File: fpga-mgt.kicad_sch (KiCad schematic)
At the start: 19 parts, among them U34 XCAU25P-2FFVB676I

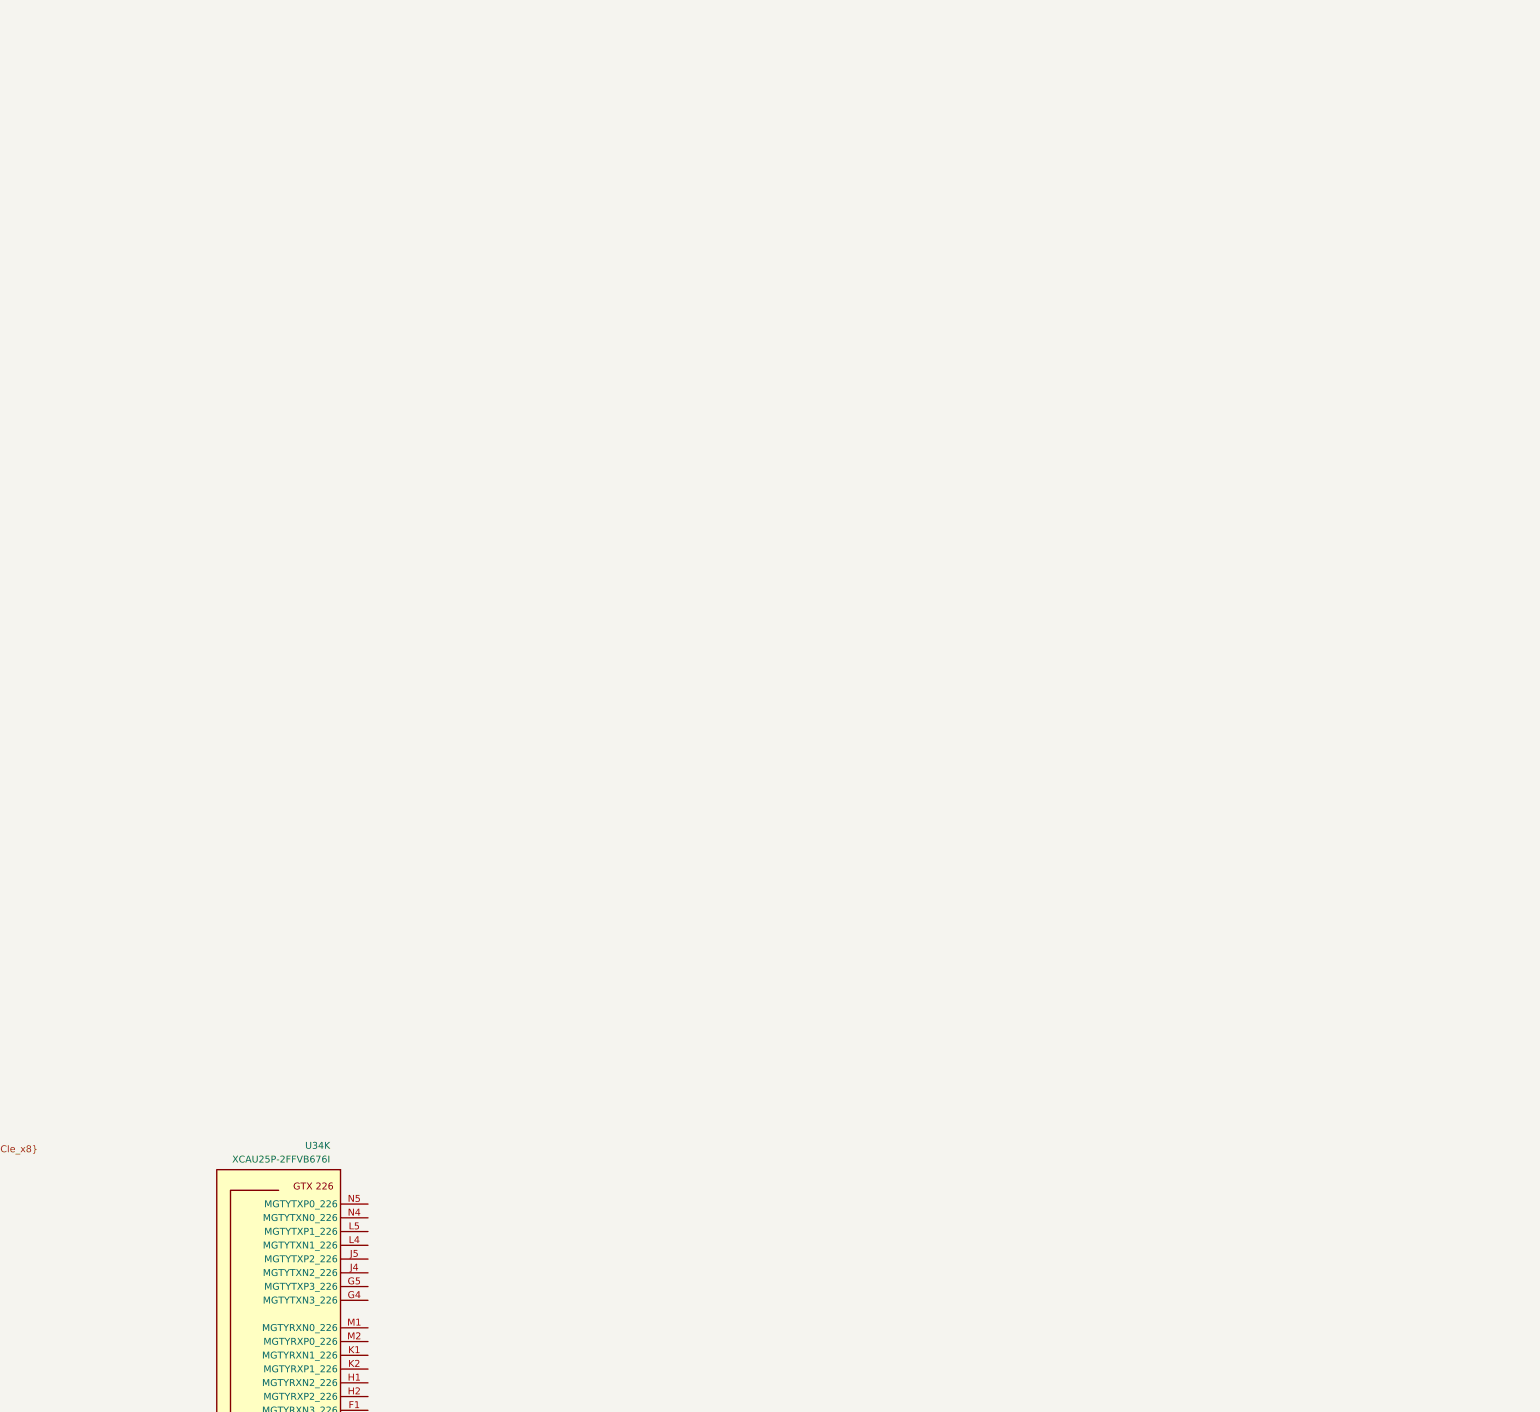
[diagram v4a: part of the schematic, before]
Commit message: [#66312] Add HDMI driver. Connect TMDS to GTH quad 226
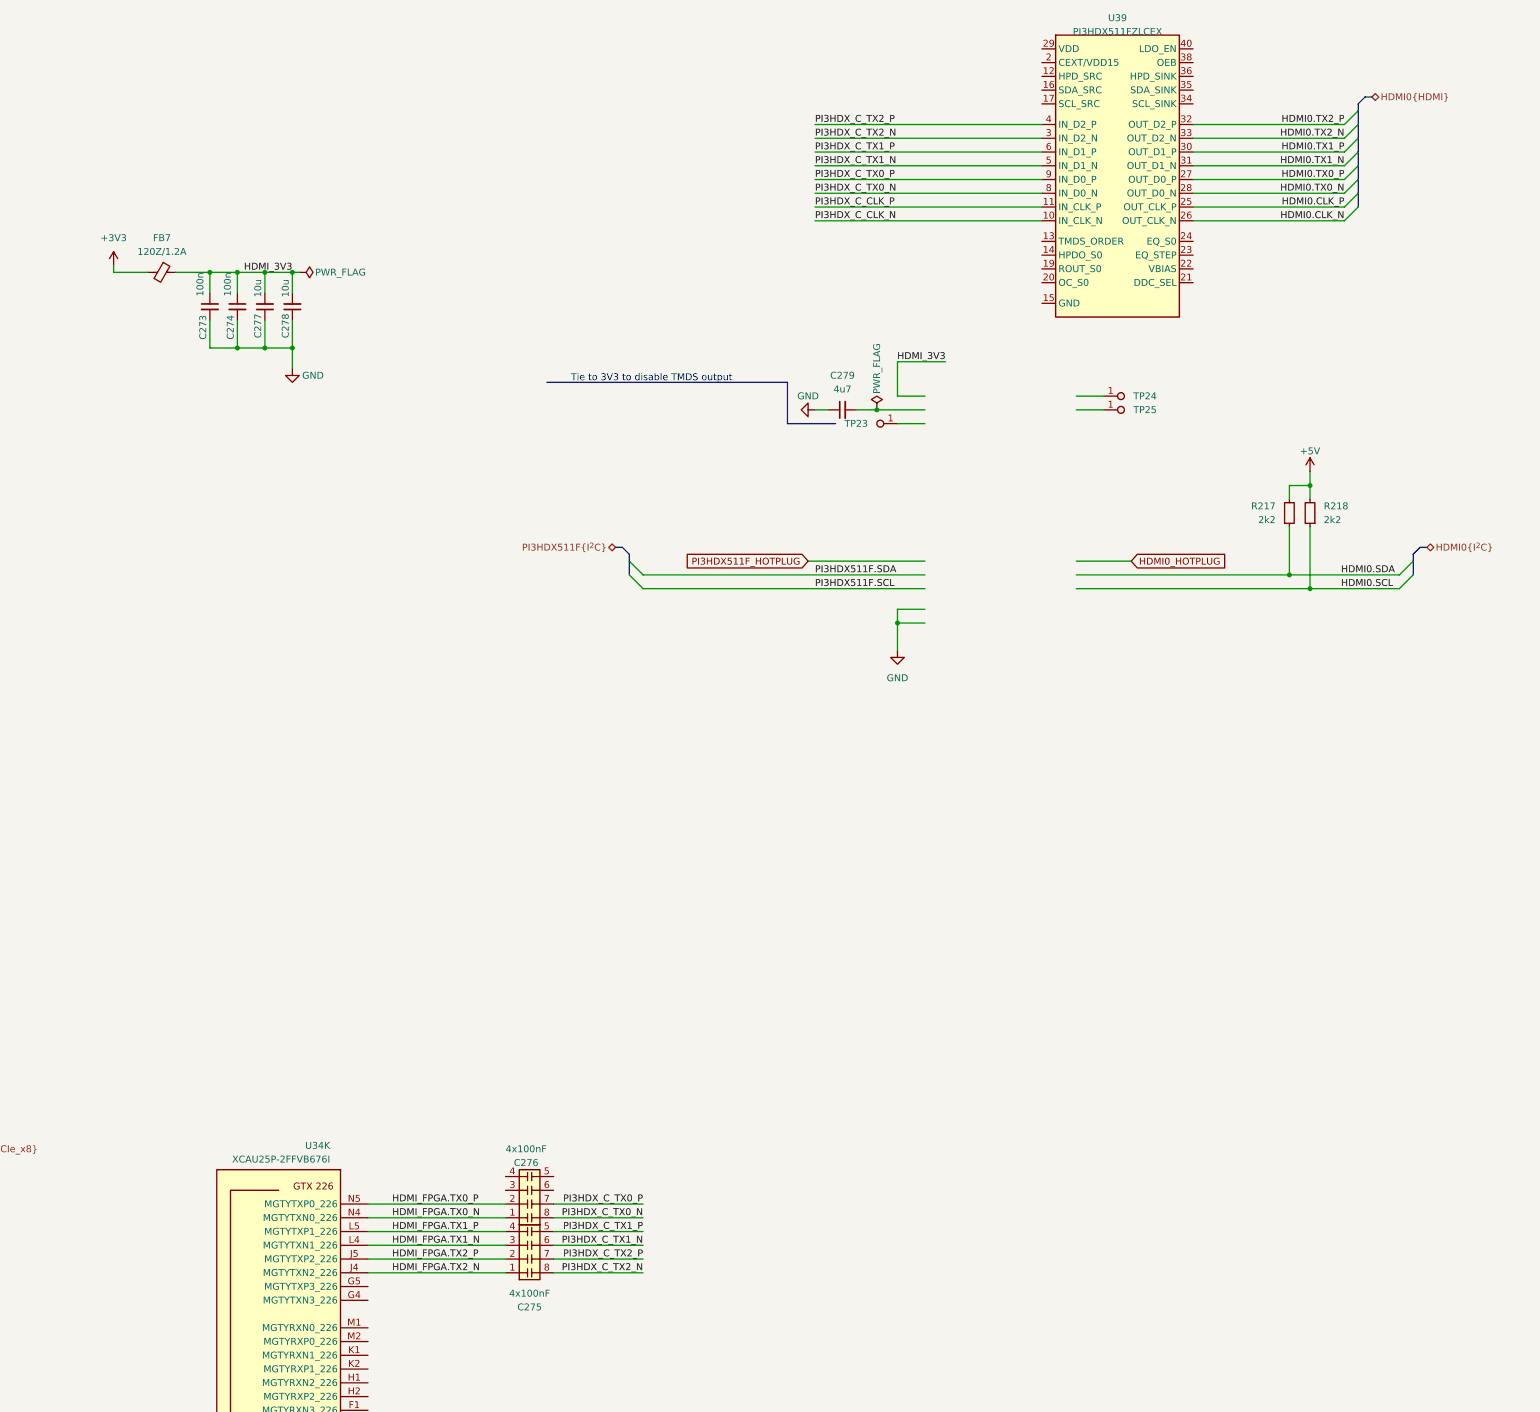
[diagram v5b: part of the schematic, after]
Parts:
- added C273, C274: C_100n_0402, antmicro-footprints:C_0402_1005Metric, symbol antmicroCapacitors0402:C_100n_0402
- added C275, C276: C_4x100nF_0508_1220Metric_array, antmicro-footprints:C_Array_0508_1220Metric, symbol antmicroCapacitorsmisc:C_4x100nF_0508_1220Metric_array
- added C277, C278: C_10u_10V_0402, antmicro-footprints:C_0402_1005Metric, symbol antmicroCapacitors0402:C_10u_10V_0402
- added C279: C_4u7_0402, antmicro-footprints:C_0402_1005Metric, symbol antmicroCapacitors0402:C_4u7_0402
- added FB7: FB_120Z_1.2A_TDK-MPZ_0402, antmicro-footprints:FB_0402_1005Metric, symbol antmicroFerriteBeadsandChips:FB_120Z_1.2A_TDK-MPZ_0402
- added R217, R218: R_2k2_0402, antmicro-footprints:R_0402_1005Metric, symbol antmicroResistors0402:R_2k2_0402
- added TP23, TP24, TP25: TP_0.75mm_SMD, antmicro-footprints:TP_SMD_0.75mm, symbol antmicroTestPoints:TP_0.75mm_SMD
- added U39: PI3HDX511FZLCEX, antmicro-footprints:QFN-40-1EP_3x6mm_Layout6x14, symbol antmicroInterfaceDriversReceiversTransceivers:PI3HDX511FZLCEX
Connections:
- net HDMI_FPGA.TX2_N: now reaches U34.J4 (MGTYTXN2_226)
- net HDMI_FPGA.TX2_N: now also C275.1 (R1.1)
- net HDMI_FPGA.TX2_P: now reaches U34.J5 (MGTYTXP2_226)
- net HDMI_FPGA.TX2_P: now also C275.2 (R2.1)
- net HDMI_FPGA.TX1_N: now reaches U34.L4 (MGTYTXN1_226)
- net HDMI_FPGA.TX1_N: now also C275.3 (R3.1)
- net HDMI_FPGA.TX1_P: now reaches U34.L5 (MGTYTXP1_226)
- net HDMI_FPGA.TX1_P: now also C275.4 (R4.1)
- net HDMI_FPGA.TX0_N: now reaches U34.N4 (MGTYTXN0_226)
- net HDMI_FPGA.TX0_N: now also C276.1 (R1.1)
- net HDMI_FPGA.TX0_P: now reaches U34.N5 (MGTYTXP0_226)
- net HDMI_FPGA.TX0_P: now also C276.2 (R2.1)
- new net +3V3: FB7.2
- new net +5V: R217.2, R218.2
- new net GND: C273.2, C274.2, C277.1, C278.1, C279.1, U39.15 (GND), U39.18 (GND), U39.37 (GND), U39.39 (GND), U39.41 (GND)
- new net HDMI0.CLK_N: U39.26 (OUT_CLK_N)
- new net HDMI0.CLK_P: U39.25 (OUT_CLK_P)
- new net HDMI0.SCL: R218.1
- new net HDMI0.SDA: R217.1
- new net HDMI0.TX0_N: U39.28 (OUT_D0_N)
- new net HDMI0.TX0_P: U39.27 (OUT_D0_P)
- new net HDMI0.TX1_N: U39.31 (OUT_D1_N)
- new net HDMI0.TX1_P: U39.30 (OUT_D1_P)
- new net HDMI0.TX2_N: U39.33 (OUT_D2_N)
- new net HDMI0.TX2_P: U39.32 (OUT_D2_P)
- new net HDMI_3V3: C273.1, C274.1, C277.2, C278.2, FB7.1
- new net PI3HDX_C_CLK_N: U39.10 (IN_CLK_N)
- new net PI3HDX_C_CLK_P: U39.11 (IN_CLK_P)
- new net PI3HDX_C_TX0_N: C276.8 (R1.2), U39.8 (IN_D0_N)
- new net PI3HDX_C_TX0_P: C276.7 (R2.2), U39.9 (IN_D0_P)
- new net PI3HDX_C_TX1_N: C275.6 (R3.2), U39.5 (IN_D1_N)
- new net PI3HDX_C_TX1_P: C275.5 (R4.2), U39.6 (IN_D1_P)
- new net PI3HDX_C_TX2_N: C275.8 (R1.2), U39.3 (IN_D2_N)
- new net PI3HDX_C_TX2_P: C275.7 (R2.2), U39.4 (IN_D2_P)
- new net VDD: U39.1 (VDD), U39.29 (VDD), U39.7 (VDD)
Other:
- note added: "Tie to 3V3 to disable TMDS output"

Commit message: [#66300] Replace HDMI output driver to SN75DP159
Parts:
- removed C277: C_10u_10V_0402, antmicro-footprints:C_0402_1005Metric, symbol antmicroCapacitors0402:C_10u_10V_0402
- removed FB7: FB_120Z_1.2A_TDK-MPZ_0402, antmicro-footprints:FB_0402_1005Metric, symbol antmicroFerriteBeadsandChips:FB_120Z_1.2A_TDK-MPZ_0402
- removed TP23: TP_0.75mm_SMD, antmicro-footprints:TP_SMD_0.75mm, symbol antmicroTestPoints:TP_0.75mm_SMD
- removed U39: PI3HDX511FZLCEX, antmicro-footprints:QFN-40-1EP_3x6mm_Layout6x14, symbol antmicroInterfaceDriversReceiversTransceivers:PI3HDX511FZLCEX
- added C277, C280, C281, C282, C284, C285, C286, C288, C289, C291: C_100n_0402, antmicro-footprints:C_0402_1005Metric, symbol antmicroCapacitors0402:C_100n_0402
- added C283, C287: C_10u_10V_0402, antmicro-footprints:C_0402_1005Metric, symbol antmicroCapacitors0402:C_10u_10V_0402
- added R219, R220: R_4k7_0402, antmicro-footprints:R_0402_1005Metric, symbol antmicroResistors0402:R_4k7_0402
- added U38: SI5319C-C-GM-ND, antmicro-footprints:QFN-36-1EP_6x6mm_P0.5mm_EP3.7x3.7mm, symbol antmicroClockTimingClockGeneratorsPLLsFrequencySynthesizers:SI5319C-C-GM-ND
- added U40: SN65DP159RGZR, antmicro-footprints:VQFN-48_7x7mm_P0.5mm_EP4.1x4.1mm, symbol antmicroInterfaceDriversReceiversTransceivers:SN65DP159RGZR
- added Y4: Resonator_114.285MHZ_ABM8, antmicro-footprints:Resonator_SMD_Abracon_ABM8G_3.2x2.5mm, symbol antmicroResonators:Resonator_114.285MHZ_ABM8
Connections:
- net GND: now also C277.2, C280.2, C281.2, C282.2, C283.1, C286.2, C287.1, C288.2, C289.2, C291.2, R219.1, U38.19 (GND), U38.20 (GND), U38.31 (GND), U38.8 (GND), U40.19 (GND), U40.30 (GND), U40.41 (GND), U40.49 (GND), U40.7 (GND), Y4.2 (SH), Y4.4 (SH)
- net HDMI_FPGA.TX0_N: now also C276.3 (R3.1); no longer C276.1 (R1.1)
- net HDMI_FPGA.TX0_P: now also C276.4 (R4.1); no longer C276.2 (R2.1)
- net HDMI_FPGA.TX1_N: now also C276.1 (R1.1); no longer C275.3 (R3.1)
- net HDMI_FPGA.TX1_P: now also C276.2 (R2.1); no longer C275.4 (R4.1)
- net HDMI_FPGA.TX2_N: now also C275.3 (R3.1); no longer C275.1 (R1.1)
- net HDMI_FPGA.TX2_P: now also C275.4 (R4.1); no longer C275.2 (R2.1)
- net PI3HDX_C_CLK_N: now also C275.8 (R1.2), U40.12 (VCC)
- net PI3HDX_C_CLK_P: now also C275.7 (R2.2), U40.11 (IN_CLK_P)
- net PI3HDX_C_TX0_N: now also C276.6 (R3.2), U40.9 (IN_D0_N); no longer C276.8 (R1.2)
- net PI3HDX_C_TX0_P: now also C276.5 (R4.2), U40.8 (IN_D0_P); no longer C276.7 (R2.2)
- net PI3HDX_C_TX1_N: now also C276.8 (R1.2), U40.6 (IN_D1_N); no longer C275.6 (R3.2)
- net PI3HDX_C_TX1_P: now also C276.7 (R2.2), U40.5 (IN_D1_P); no longer C275.5 (R4.2)
- net PI3HDX_C_TX2_N: now also C275.6 (R3.2), U40.3 (IN_D2_N); no longer C275.8 (R1.2)
- net PI3HDX_C_TX2_P: now also C275.5 (R4.2), U40.2 (IN_D2_P); no longer C275.7 (R2.2)
- net HDMI_3V3 renamed +1V1
- net +1V1: now also C277.1, C280.1, C281.1, C282.1, C283.2, C286.1, C287.2, C288.1, C289.1, C291.1, R220.2, U38.10 (VDD), U38.32 (VDD), U38.5 (VDD), U40.12 (VCC), U40.14 (VDD), U40.23 (VDD), U40.24 (VDD), U40.37 (VDD), U40.43 (VCC), U40.48 (VDD)
- new net: R220.1, U38.1 (~{RST})
- new net: R219.2, U38.21 (CS)
- new net: U38.24 (A0), U38.25 (A1), U38.26 (A2_~{SS}), U38.36 (CMODE)
- new net HDMI_OUT_CLK_C_N: C285.1
- new net HDMI_OUT_CLK_C_P: C284.1
- new net HDMI_OUT_CLK_N: C285.2, U38.29 (CKOUT-)
- new net HDMI_OUT_CLK_P: C284.2, U38.28 (CKOUT+)
- new net XA: U38.6 (XA), Y4.1
- new net XB: U38.7 (XB), Y4.3
- no-connect marks 6 -> 12
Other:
- note removed: "Tie to 3V3 to disable TMDS output"
- moved on the sheet: C273, C274, C275, C276, C279, R217, R218, TP24, TP25

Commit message: [#66727] Finish connecting HDMI driver. Add SD card logic level converter. Add SD 3.0 support
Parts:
- removed C273, C274, C277, C280, C281, C282, C284, C288: C_100n_0402, antmicro-footprints:C_0402_1005Metric, symbol antmicroCapacitors0402:C_100n_0402
- removed C275, C276: C_4x100nF_0508_1220Metric_array, antmicro-footprints:C_Array_0508_1220Metric, symbol antmicroCapacitorsmisc:C_4x100nF_0508_1220Metric_array
- removed C278, C283, C287: C_10u_10V_0402, antmicro-footprints:C_0402_1005Metric, symbol antmicroCapacitors0402:C_10u_10V_0402
- removed C279: C_4u7_0402, antmicro-footprints:C_0402_1005Metric, symbol antmicroCapacitors0402:C_4u7_0402
- removed R217, R218: R_2k2_0402, antmicro-footprints:R_0402_1005Metric, symbol antmicroResistors0402:R_2k2_0402
- removed R219, R220: R_4k7_0402, antmicro-footprints:R_0402_1005Metric, symbol antmicroResistors0402:R_4k7_0402
- removed TP24, TP25: TP_0.75mm_SMD, antmicro-footprints:TP_SMD_0.75mm, symbol antmicroTestPoints:TP_0.75mm_SMD
- removed U38: SI5319C-C-GM-ND, antmicro-footprints:QFN-36-1EP_6x6mm_P0.5mm_EP3.7x3.7mm, symbol antmicroClockTimingClockGeneratorsPLLsFrequencySynthesizers:SI5319C-C-GM-ND
- removed U40: SN65DP159RGZR, antmicro-footprints:VQFN-48_7x7mm_P0.5mm_EP4.1x4.1mm, symbol antmicroInterfaceDriversReceiversTransceivers:SN65DP159RGZR
- added C275, C276, C279, C287, C290, C292, C293: C_100n_0402, antmicro-footprints:C_0402_1005Metric, symbol antmicroCapacitors0402:C_100n_0402
- added C288: C_10u_10V_0402, antmicro-footprints:C_0402_1005Metric, symbol antmicroCapacitors0402:C_10u_10V_0402
- added R70, R74: R_4k7_0402, antmicro-footprints:R_0402_1005Metric, symbol antmicroResistors0402:R_4k7_0402
- added U39: SI5319C-C-GM-ND, antmicro-footprints:QFN-36-1EP_6x6mm_P0.5mm_EP3.7x3.7mm, symbol antmicroClockTimingClockGeneratorsPLLsFrequencySynthesizers:SI5319C-C-GM-ND
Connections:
- net GND: now also C285.2, C287.2, C288.1, R74.1, U39.19 (GND), U39.20 (GND), U39.31 (GND), U39.8 (GND); no longer C289.2, C291.2
- net HDMI0.TX0_N: now also C276.1
- net HDMI0.TX0_P: now also C275.1
- net HDMI0.TX1_N: now also C290.1
- net HDMI0.TX1_P: now also C279.1
- net HDMI0.TX2_N: now also C293.1
- net HDMI0.TX2_P: now also C292.1
- net HDMI_FPGA.TX0_N: now also C276.2
- net HDMI_FPGA.TX0_P: now also C275.2
- net HDMI_FPGA.TX1_N: now also C290.2
- net HDMI_FPGA.TX1_P: now also C279.2
- net HDMI_FPGA.TX2_N: now also C293.2
- net HDMI_FPGA.TX2_P: now also C292.2
- net HDMI_OUT_CLK_C_N: now also C291.1, U34.P6 (MGTREFCLK0N_226); no longer C285.1
- net HDMI_OUT_CLK_C_P: now also C289.1, U34.P7 (MGTREFCLK0P_226)
- net HDMI_OUT_CLK_N: now also C291.2, U39.29 (CKOUT-); no longer C285.2
- net HDMI_OUT_CLK_P: now also C289.2, U39.28 (CKOUT+)
- net XA: now also U39.6 (XA)
- net XB: now also U39.7 (XB)
- removed net +1V1: C286.1, C289.1, C291.1
- new net: R70.1, U39.1 (~{RST})
- new net: R74.2, U39.21 (CS)
- new net: U39.24 (A0), U39.25 (A1), U39.26 (A2_~{SS}), U39.36 (CMODE)
- new net +3V3: C285.1, C286.1, C287.1, C288.2, R70.2, U39.10 (VDD), U39.32 (VDD), U39.5 (VDD)
- new net HDMI_CTL.SCL: U39.22 (SCL)
- new net HDMI_CTL.SDA: U39.23 (SDA_SDO)
- no-connect marks 12 -> 11
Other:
- note added: "HDMI"
- note added: "PCIe 3.0 x8"
- moved on the sheet: U34K
